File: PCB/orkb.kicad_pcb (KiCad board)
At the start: 2 copper layers, 304.3 x 117.2 mm, 82 parts, among them J1 USB_C_Receptacle_USB2.0, P1 OLED, SW1 MXHS, SW10 MXHS, SW11 MXHS, SW12 MXHS, SW13 MXHS, SW14 MXHS, SW15 MXHS, SW16 MXHS, SW17 MXHS, SW18 MXHS, SW19 MXHS, SW2 MXHS, SW20 MXHS, SW21 MXHS, SW22 MXHS, SW23 MXHS, SW3 MXHS, SW4 MXHS, SW5 MXHS, SW6 MXHS, SW7 MXHS, SW8 MXHS, SW9 MXHS, U1 ProMicro, U2 SRV05-4, U3 SRV05-4

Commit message: Reset switch repositioning and labeling
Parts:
- moved RES1 79.6 mm to (66.5, 126.2), turned to 90 degrees
- moved RES2 79.6 mm to (66.5, 126.2), turned to -90 degrees
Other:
- board size 304.3 x 117.2 mm -> 148.5 x 113.3 mm
- board text added: "ORCA"
- board text removed: "ENCODER HERE"
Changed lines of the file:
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@@
 	(footprint "SplitKeyboard_Common:YTS-A002"
 		(layer "F.Cu")
-		(at 92.837 51.054)
+		(at 66.548 126.238 90)
 		(property "Reference" "RES1"
-			(at 0 -3.2 0)
+			(at 0 -3.2 90)
 			(unlocked yes)
 			(layer "F.SilkS")
@@
 		)
 		(property "Value" "TS-A002_TactileSW"
-			(at -1.27 -5.08 0)
+			(at -1.27 -5.080001 90)
 			(unlocked yes)
 			(layer "F.Fab")
@@
 		)
 		(property "Footprint" "SplitKeyboard_Common:YTS-A002"
-			(at 0 0 0)
+			(at 0 0 90)
 			(unlocked yes)
 			(layer "F.Fab")
@@
 		)
 		(property "Datasheet" ""
-			(at 0 0 0)
+			(at 0 0 90)
 			(unlocked yes)
 			(layer "F.Fab")
@@
 		)
 		(property "Description" ""
-			(at 0 0 0)
+			(at 0 0 90)
 			(unlocked yes)
 			(layer "F.Fab")
@@
 		)
 		(property "LCSC" "C2888934"
-			(at 0 0 0)
+			(at 0 0 90)
 			(layer "F.Fab")
 			(hide yes)
@@
 		(sheetfile "orkb.kicad_sch")
 		(attr smd)
-		(fp_rect
-			(start -2.4 -0.85)
-			(end 2.4 1.55)
+		(fp_poly
+			(pts
+				(xy -0.95 -2.1) (xy 0.95 -2.1) (xy 0.95 -0.9) (xy -0.95 -0.9)
+			)
 			(stroke
 				(width 0.1)
@@
 			(layer "Dwgs.User")
 		)
-		(fp_rect
-			(start -0.95 -2.1)
-			(end 0.95 -0.9)
+		(fp_poly
+			(pts
+				(xy -2.4 -0.849999) (xy 2.4 -0.850001) (xy 2.400001 1.55) (xy -2.399999 1.550001)
+			)
 			(stroke
 				(width 0.1)
@@
 			(layer "Dwgs.User")
 		)
-		(fp_rect
-			(start -3 -2.25)
-			(end 3 1.95)
+		(fp_poly
+			(pts
+				(xy -2.999999 -2.25) (xy 3.000001 -2.249999) (xy 3.000001 1.95) (xy -2.999999 1.950001)
+			)
 			(stroke
 				(width 0.1)
@@
 		)
 		(pad "" np_thru_hole circle
-			(at -0.85 0)
+			(at -0.85 0 90)
 			(size 0.7 0.7)
 			(drill 0.7)
@@
 		)
 		(pad "" np_thru_hole circle
-			(at 0.85 0)
+			(at 0.85 0 90)
 			(size 0.7 0.7)
 			(drill 0.7)
@@
 		)
 		(pad "1" smd roundrect
-			(at -2 1.35)
+			(at -2 1.349999 90)
 			(size 0.6 1.1)
 			(layers "F.Cu" "F.Paste" "F.Mask")
@@
 		)
 		(pad "2" smd roundrect
-			(at 2 1.35)
+			(at 1.999999 1.350001 90)
 			(size 0.6 1.1)
 			(layers "F.Cu" "F.Paste" "F.Mask")
@@
 		)
 		(pad "3" smd roundrect
-			(at -2.475 -0.35)
+			(at -2.475 -0.35 90)
 			(size 0.95 1.1)
 			(layers "F.Cu" "F.Paste" "F.Mask")
@@
 		)
 		(pad "3" smd roundrect
-			(at 2.54 -0.35)
+			(at 2.540001 -0.350001 90)
 			(size 0.95 1.1)
 			(layers "F.Cu" "F.Paste" "F.Mask")
@@
 	(footprint "SplitKeyboard_Common:YTS-A002"
 		(layer "B.Cu")
-		(at 92.837 51.054 180)
+		(at 66.548 126.238 -90)
 		(property "Reference" "RES2"
-			(at 0 3.2 0)
+			(at 0 3.2 90)
 			(unlocked yes)
 			(layer "B.SilkS")
@@
 		)
 		(property "Value" "TS-A002_TactileSW"
-			(at -1.27 5.08 0)
+			(at -1.269999 5.08 90)
 			(unlocked yes)
 			(layer "B.Fab")
@@
 		)
 		(property "Footprint" "SplitKeyboard_Common:YTS-A002"
-			(at 0 0 0)
+			(at 0 0 90)
 			(unlocked yes)
 			(layer "B.Fab")
@@
 		)
 		(property "Datasheet" ""
-			(at 0 0 0)
+			(at 0 0 90)
 			(unlocked yes)
 			(layer "B.Fab")
@@
 		)
 		(property "Description" ""
-			(at 0 0 0)
+			(at 0 0 90)
 			(unlocked yes)
 			(layer "B.Fab")
@@
 		)
 		(property "LCSC" "C2888934"
-			(at 0 0 0)
+			(at 0 0 90)
 			(layer "B.Fab")
 			(hide yes)
@@
 		(sheetfile "orkb.kicad_sch")
 		(attr smd)
-		(fp_rect
-			(start 2.4 -1.55)
-			(end -2.4 0.85)
+		(fp_poly
+			(pts
+				(xy 0.95 0.9) (xy -0.95 0.9) (xy -0.95 2.1) (xy 0.95 2.1)
+			)
 			(stroke
 				(width 0.1)
@@
 			(layer "Dwgs.User")
 		)
-		(fp_rect
-			(start 0.95 0.9)
-			(end -0.95 2.1)
+		(fp_poly
+			(pts
+				(xy 2.399999 -1.550001) (xy -2.400001 -1.55) (xy -2.4 0.850001) (xy 2.4 0.849999)
+			)
 			(stroke
 				(width 0.1)
@@
 			(layer "Dwgs.User")
 		)
-		(fp_rect
-			(start 3 -1.95)
-			(end -3 2.25)
+		(fp_poly
+			(pts
+				(xy 2.999999 -1.950001) (xy -3.000001 -1.95) (xy -3.000001 2.249999) (xy 2.999999 2.25)
+			)
 			(stroke
 				(width 0.1)
@@
 		)
 		(pad "" np_thru_hole circle
-			(at -0.85 0 180)
+			(at -0.85 0 270)
 			(size 0.7 0.7)
 			(drill 0.7)
@@
 		)
 		(pad "" np_thru_hole circle
-			(at 0.85 0 180)
+			(at 0.85 0 270)
 			(size 0.7 0.7)
 			(drill 0.7)
@@
 		)
 		(pad "1" smd roundrect
-			(at -2 -1.35 180)
+			(at -1.999999 -1.350001 270)
 			(size 0.6 1.1)
 			(layers "B.Cu" "B.Paste" "B.Mask")
@@
 		)
 		(pad "2" smd roundrect
-			(at 2 -1.35 180)
+			(at 2 -1.349999 270)
 			(size 0.6 1.1)
 			(layers "B.Cu" "B.Paste" "B.Mask")
@@
 		)
 		(pad "3" smd roundrect
-			(at -2.475 0.35 180)
+			(at -2.475 0.35 270)
 			(size 0.95 1.1)
 			(layers "B.Cu" "B.Paste" "B.Mask")
@@
 		)
 		(pad "3" smd roundrect
-			(at 2.54 0.35 180)
+			(at 2.54 0.349999 270)
 			(size 0.95 1.1)
 			(layers "B.Cu" "B.Paste" "B.Mask")
@@
 		)
 	)
+	(gr_rect
+		(start 136.779 99.568)
+		(end 154.813 105.156)
+		(stroke
+			(width 0.1)
+			(type default)
+		)
+		(fill none)
+		(layer "F.SilkS")
+	)
 	(gr_line
 		(start 65.278 51.054)
@@
 	)
 	(gr_arc
-		(start 349.25 58.42)
-		(mid 348.351974 58.048026)
-		(end 347.98 57.15)
-		(stroke
-			(width 0.05)
-			(type default)
-		)
-		(layer "Edge.Cuts")
-	)
-	(gr_arc
 		(start 149.225 107.696)
 		(mid 149.596974 106.797974)
@@
 		(layer "Edge.Cuts")
 	)
-	(gr_line
-		(start 369.57 57.15)
-		(end 369.57 38.1)
-		(stroke
-			(width 0.05)
-			(type default)
-		)
-		(layer "Edge.Cuts")
-	)
 	(gr_arc
 		(start 115.951 48.514)
@@
 	)
 	(gr_line
-		(start 368.3 58.42)
-		(end 349.25 58.42)
-		(stroke
-			(width 0.05)
-			(type default)
-		)
-		(layer "Edge.Cuts")
-	)
-	(gr_line
 		(start 136.271 40.767)
 		(end 155.321 40.767)
@@
 	)
 	(gr_arc
-		(start 369.57 57.15)
-		(mid 369.198026 58.048026)
-		(end 368.3 58.42)
-		(stroke
-			(width 0.05)
-			(type default)
-		)
-		(layer "Edge.Cuts")
-	)
-	(gr_arc
 		(start 135.001 42.037)
 		(mid 135.372974 41.138974)
@@
 		(layer "Edge.Cuts")
 	)
-	(gr_arc
-		(start 347.98 38.1)
-		(mid 348.351974 37.201974)
-		(end 349.25 36.83)
-		(stroke
-			(width 0.05)
-			(type default)
-		)
-		(layer "Edge.Cuts")
-	)
 	(gr_line
 		(start 157.861 46.736)
@@
 		(layer "Edge.Cuts")
 	)
-	(gr_line
-		(start 347.98 38.1)
-		(end 347.98 57.15)
-		(stroke
-			(width 0.05)
-			(type default)
-		)
-		(layer "Edge.Cuts")
-	)
 	(gr_arc
 		(start 157.861 46.736)
@@
 		(layer "Edge.Cuts")
 	)
-	(gr_line
-		(start 368.3 36.83)
-		(end 349.25 36.83)
-		(stroke
-			(width 0.05)
-			(type default)
-		)
-		(layer "Edge.Cuts")
-	)
 	(gr_arc
 		(start 155.321 40.767)
@@
 	)
 	(gr_arc
-		(start 368.3 36.83)
-		(mid 369.198026 37.201974)
-		(end 369.57 38.1)
-		(stroke
-			(width 0.05)
-			(type default)
-		)
-		(layer "Edge.Cuts")
-	)
-	(gr_arc
 		(start 115.951 48.514)
 		(mid 116.322974 47.615974)
@@
 		(layer "Edge.Cuts")
 	)
-	(gr_text "ENCODER HERE"
-		(at 65.278 122.191501 0)
-		(layer "Edge.Cuts")
-		(effects
-			(font
-				(size 1.5 1.5)
-				(thickness 0.3)
-				(bold yes)
-			)
-			(justify left bottom)
-		)
-	)
-	(gr_text "ENCODER HERE"
-		(at 73.66 130.302 90)
-		(layer "Edge.Cuts")
+	(gr_text "ORCA"
+		(at 137.795 104.775 0)
+		(layer "F.SilkS")
 		(effects
 			(font
-				(size 1.5 1.5)
-				(thickness 0.3)
-				(bold yes)
+				(size 4 4)
+				(thickness 0.1)
 			)
 			(justify left bottom)

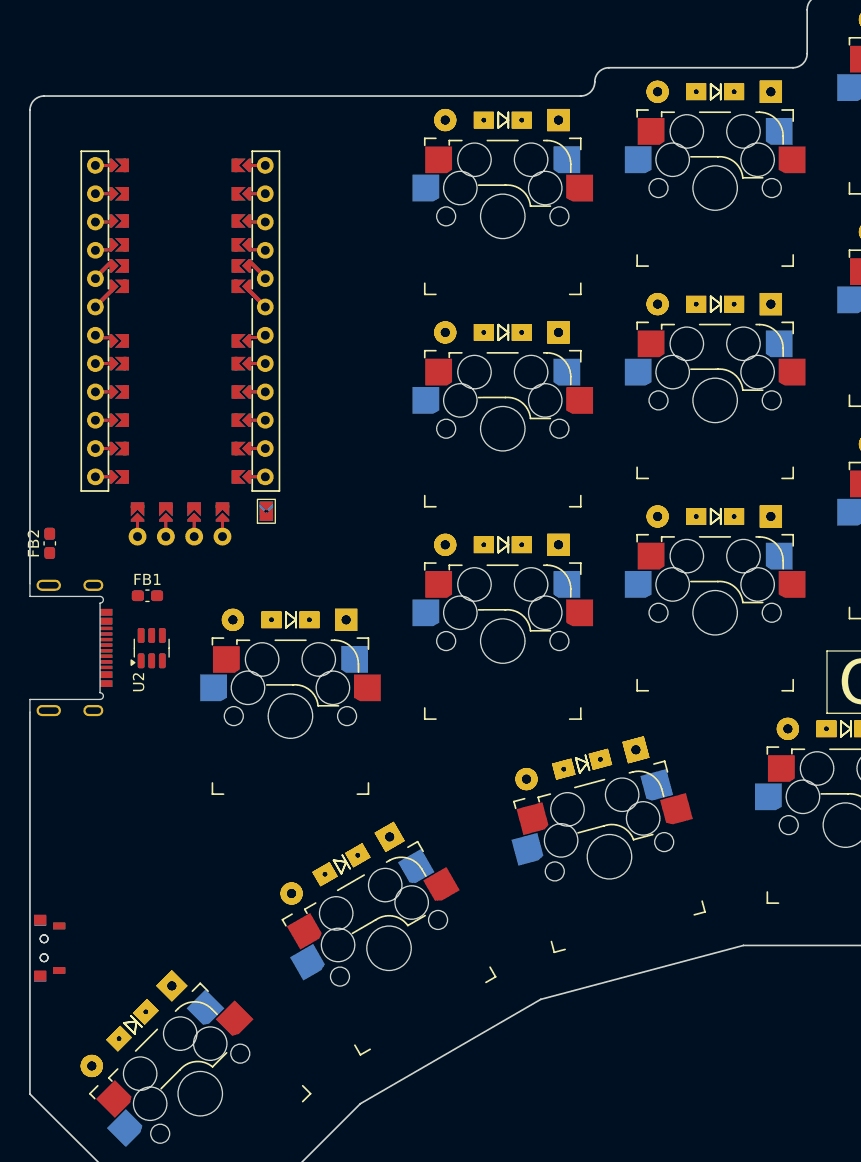
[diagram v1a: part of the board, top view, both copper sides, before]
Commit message: Changing layout and adding space for a three way switch
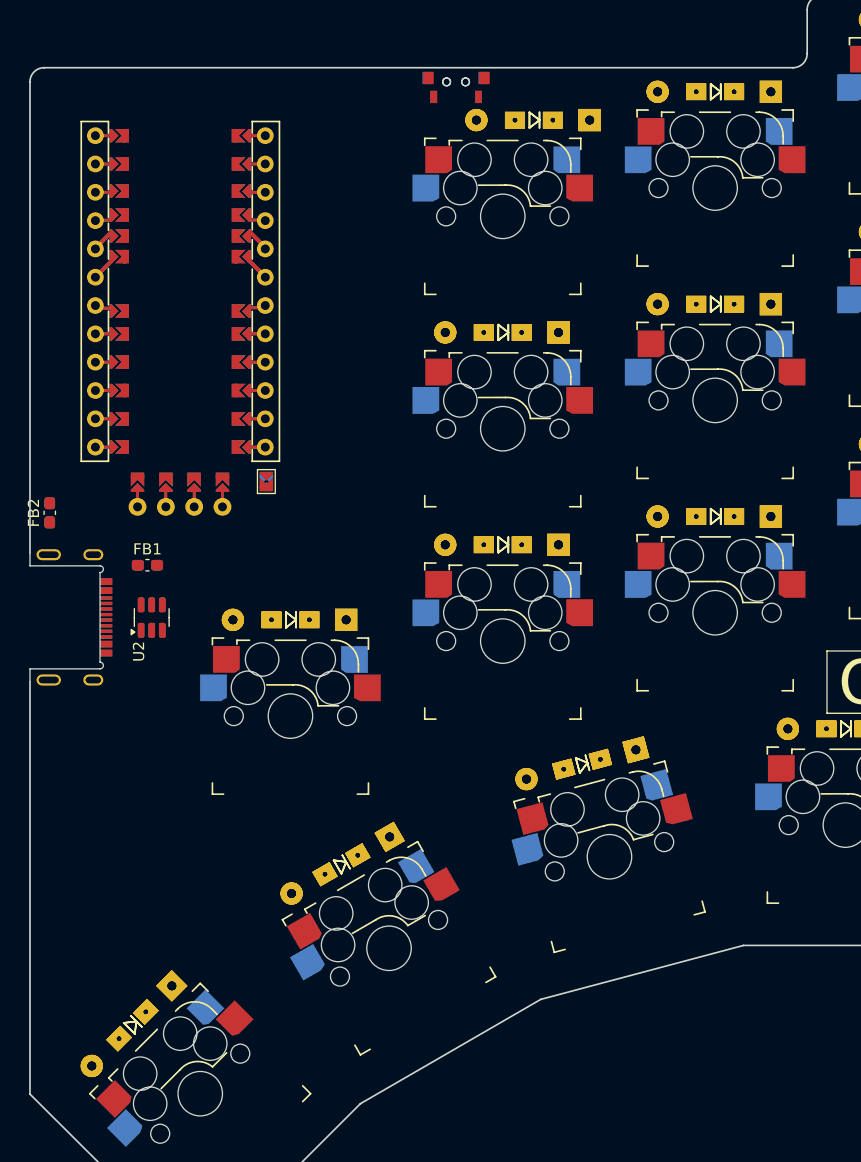
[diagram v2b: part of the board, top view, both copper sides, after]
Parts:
- moved RES1 86.1 mm to (103.5, 48.5), turned to 0 degrees
- moved RES2 86.1 mm to (103.5, 48.5), turned to 180 degrees
- moved D1 2.79 mm to (110.5, 51.9)
- moved D23 2.79 mm to (110.5, 51.9)
- moved FB1 2.74 mm to (75.8, 91.9)
- moved FB2 2.74 mm to (67.1, 87.2)
- moved FB3 2.74 mm to (75.8, 91.9)
- moved FB4 2.74 mm to (67.1, 87.2)
- moved J1 2.74 mm to (65.8, 96.6)
- moved U2 2.74 mm to (76.2, 96.6)
- moved U3 2.74 mm to (76.2, 96.6)
- moved JP1 2.67 mm to (86.5, 84.4)
- moved JP2 2.67 mm to (86.5, 84.4)
- moved P1 2.67 mm to (78.7, 68.1)
- moved U1 2.67 mm to (78.8, 67.3)
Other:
- outline, holes or cut-outs redrawn

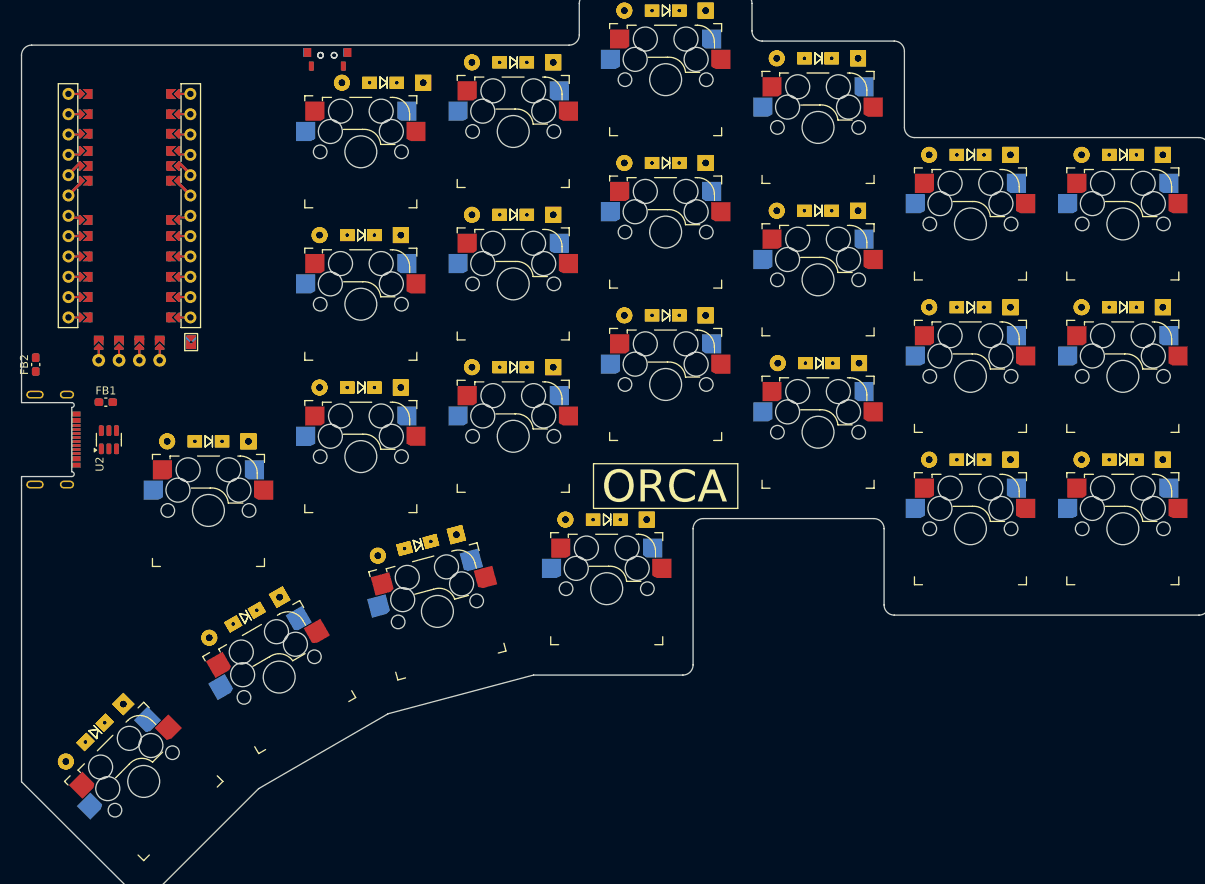
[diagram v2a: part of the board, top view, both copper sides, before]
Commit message: Updated PCB with LED and switch
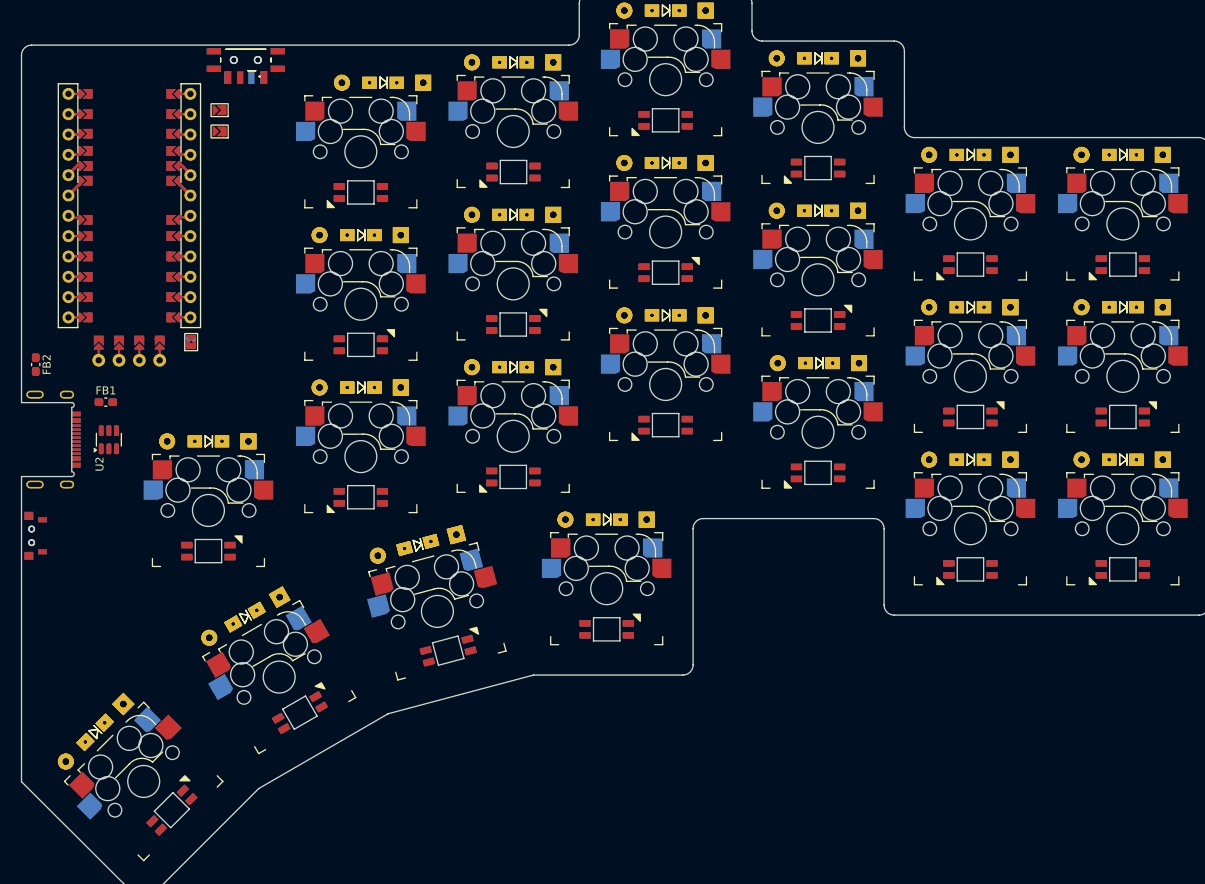
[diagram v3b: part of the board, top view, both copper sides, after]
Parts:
- added JP3: Jumper_2_Open, SplitKeyboard_Common:Jumper_min_v2, F.Cu at (90.0, 58.0)
- added JP4: Jumper_2_Open, SplitKeyboard_Common:Jumper_min_v2, F.Cu at (90.0, 55.4)
- added LED1: SK6803MINI-E, SplitKeyboard_Common:MX_SK6812MINI-E_REVERSIBLE, F.Cu at (107.7, 65.7)
- added LED10: SK6803MINI-E, SplitKeyboard_Common:MX_SK6812MINI-E_REVERSIBLE, F.Cu at (164.8, 81.7)
- added LED11: SK6803MINI-E, SplitKeyboard_Common:MX_SK6812MINI-E_REVERSIBLE, F.Cu at (183.9, 93.7)
- added LED12: SK6803MINI-E, SplitKeyboard_Common:MX_SK6812MINI-E_REVERSIBLE, F.Cu at (202.9, 93.7)
- added LED13: SK6803MINI-E, SplitKeyboard_Common:MX_SK6812MINI-E_REVERSIBLE, B.Cu at (107.7, 103.8)
- added LED14: SK6803MINI-E, SplitKeyboard_Common:MX_SK6812MINI-E_REVERSIBLE, B.Cu at (126.7, 101.2)
- added LED15: SK6803MINI-E, SplitKeyboard_Common:MX_SK6812MINI-E_REVERSIBLE, B.Cu at (145.8, 94.7)
- added LED16: SK6803MINI-E, SplitKeyboard_Common:MX_SK6812MINI-E_REVERSIBLE, B.Cu at (164.8, 100.7)
- added LED17: SK6803MINI-E, SplitKeyboard_Common:MX_SK6812MINI-E_REVERSIBLE, B.Cu at (183.9, 112.8)
- added LED18: SK6803MINI-E, SplitKeyboard_Common:MX_SK6812MINI-E_REVERSIBLE, B.Cu at (202.9, 112.8)
- added LED19: SK6803MINI-E, SplitKeyboard_Common:MX_SK6812MINI-E_REVERSIBLE, F.Cu at (88.6, 110.5)
- added LED2: SK6803MINI-E, SplitKeyboard_Common:MX_SK6812MINI-E_REVERSIBLE, F.Cu at (126.8, 63.1)
- added LED20: SK6803MINI-E, SplitKeyboard_Common:MX_SK6812MINI-E_REVERSIBLE, F.Cu at (84.1, 142.9)
- added LED21: SK6803MINI-E, SplitKeyboard_Common:MX_SK6812MINI-E_REVERSIBLE, F.Cu at (100.1, 130.7)
- added LED22: SK6803MINI-E, SplitKeyboard_Common:MX_SK6812MINI-E_REVERSIBLE, F.Cu at (118.6, 122.9)
- added LED23: SK6803MINI-E, SplitKeyboard_Common:MX_SK6812MINI-E_REVERSIBLE, F.Cu at (138.4, 120.3)
- added LED3: SK6803MINI-E, SplitKeyboard_Common:MX_SK6812MINI-E_REVERSIBLE, F.Cu at (145.8, 56.6)
- added LED4: SK6803MINI-E, SplitKeyboard_Common:MX_SK6812MINI-E_REVERSIBLE, F.Cu at (164.8, 62.6)
- added LED5: SK6803MINI-E, SplitKeyboard_Common:MX_SK6812MINI-E_REVERSIBLE, F.Cu at (183.9, 74.7)
- added LED6: SK6803MINI-E, SplitKeyboard_Common:MX_SK6812MINI-E_REVERSIBLE, F.Cu at (202.9, 74.7)
- added LED7: SK6803MINI-E, SplitKeyboard_Common:MX_SK6812MINI-E_REVERSIBLE, F.Cu at (107.7, 84.7)
- added LED8: SK6803MINI-E, SplitKeyboard_Common:MX_SK6812MINI-E_REVERSIBLE, F.Cu at (126.7, 82.2)
- added LED9: SK6803MINI-E, SplitKeyboard_Common:MX_SK6812MINI-E_REVERSIBLE, F.Cu at (145.8, 75.7)
- added SW24: MSK12C02, SplitKeyboard_Common:MSK12C02, F.Cu at (93.3, 49.1)
- added SW25: MSK12C02, SplitKeyboard_Common:MSK12C02, B.Cu at (93.3, 49.1)
- moved RES1 70.5 mm to (66.5, 108.6), turned to 90 degrees
- moved RES2 70.5 mm to (66.5, 108.6), turned to -90 degrees
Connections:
- U1 pad 1: unconnected-(U1-TX0/PD3-Pad1)_1 -> LED
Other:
- board text removed: "ORCA"
